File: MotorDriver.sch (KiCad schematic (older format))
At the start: 3 parts, among them P3 +12V, P4 MA, P5 MB

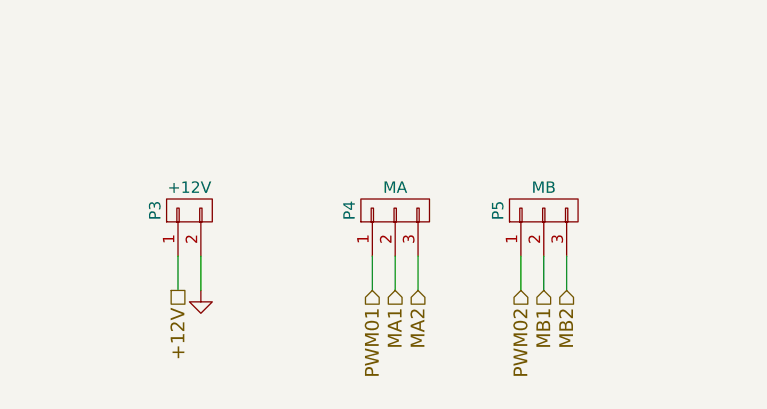
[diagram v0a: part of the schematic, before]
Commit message: Changes to be committed: 	new file:   78LXXSOT89.pdf 	modified:   Control.sch 	modified:   Debugger.sch 	modified:   MotorDriver.sch 	modified:   PS.sch 	modified:   Sensor.sch 	new file:   XL6009-Schematic-Diagram.pdf 	modified:   main-cache.lib 	new file:   main.cmp 	new file:   main.kicad_pcb 	new file:   main.net 	modified:   main.pro 	modified:   main.sch
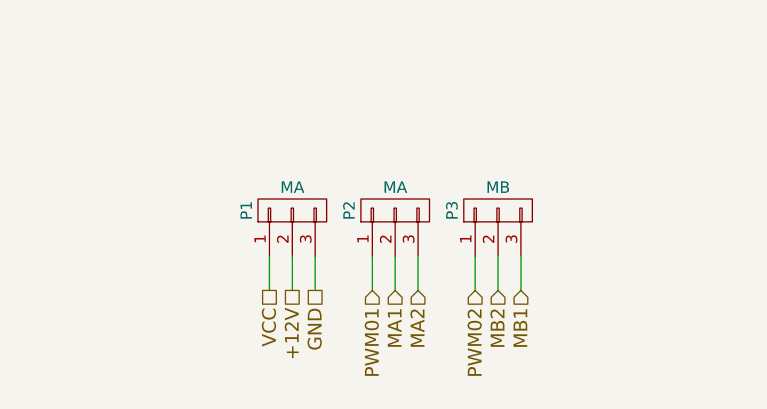
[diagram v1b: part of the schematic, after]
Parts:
- removed P3: +12V, symbol CONN_01X02
- added P1: MA, Pin_Headers:Pin_Header_Straight_1x03, symbol CONN_01X03
- P2: renamed from P4; footprint (none) -> Pin_Headers:Pin_Header_Straight_1x03
- P3: renamed from P5; footprint (none) -> Pin_Headers:Pin_Header_Straight_1x03
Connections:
- net +12V: now also P1.2 (P2)
- net GND: now also P1.3 (P3)
- net MB1: now also P3.3 (P3); no longer P3.2 (P2)
- net MB2: now also P3.2 (P2); no longer P3.3 (P3)
- new net VCC: P1.1 (P1)
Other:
- moved on the sheet: P3
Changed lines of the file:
@@
 EESchema Schematic File Version 2
+LIBS:main-rescue
 LIBS:power
 LIBS:device
@@
 LIBS:contrib
 LIBS:main-cache
+LIBS:tcrt5000
 EELAYER 25 0
 EELAYER END
 $Descr A4 11693 8268
 encoding utf-8
-Sheet 3 6
+Sheet 2 6
 Title ""
 Date ""
@@
 FC BE 3D D5 51 7A EF CF B9 F4 3C 34 7D D1 30 37 C2 0E 7F 80 58 F1 33 ED 6A 46 BF 3F CB 91 FE BE
 6F 63 8E 3F 36 CC D7 84 73 CC F1 9C 31 5F 13 CE 31 C7 73 C6 DC 08 E7 98 E3 39 63 6E 84 73 CC F1
-9C F1 FF 03 32 A2 CC 28 D8 D1 50 57 00 00 00 00 49 45 4E 44 AE 42 60 82 11
+9C F1 FF 03 32 A2 CC 28 D8 D1 50 57 00 00 00 00 49 45 4E 44 AE 42 60 82 31
 EndData
 $EndBitmap
 $Comp
-L CONN_01X02 P3
-U 1 1 558D4ABF
-P 1500 3350
-F 0 "P3" H 1500 3500 50  0000 C CNN
-F 1 "+12V" V 1600 3350 50  0000 C CNN
-F 2 "" H 1500 3350 60  0000 C CNN
-F 3 "" H 1500 3350 60  0000 C CNN
-	1    1500 3350
-	0    -1   -1   0
-$EndComp
-$Comp
-L CONN_01X03 P4
+L CONN_01X03 P2
 U 1 1 558D4B4A
 P 2400 3350
-F 0 "P4" H 2400 3550 50  0000 C CNN
+F 0 "P2" H 2400 3550 50  0000 C CNN
 F 1 "MA" V 2500 3350 50  0000 C CNN
-F 2 "" H 2400 3350 60  0000 C CNN
+F 2 "Pin_Headers:Pin_Header_Straight_1x03" H 2400 3350 60  0001 C CNN
 F 3 "" H 2400 3350 60  0000 C CNN
 	1    2400 3350
@@
 $EndComp
 $Comp
-L CONN_01X03 P5
+L CONN_01X03 P3
 U 1 1 558D4B7D
-P 3050 3350
-F 0 "P5" H 3050 3550 50  0000 C CNN
-F 1 "MB" V 3150 3350 50  0000 C CNN
-F 2 "" H 3050 3350 60  0000 C CNN
-F 3 "" H 3050 3350 60  0000 C CNN
-	1    3050 3350
+P 2850 3350
+F 0 "P3" H 2850 3550 50  0000 C CNN
+F 1 "MB" V 2950 3350 50  0000 C CNN
+F 2 "Pin_Headers:Pin_Header_Straight_1x03" H 2850 3350 60  0001 C CNN
+F 3 "" H 2850 3350 60  0000 C CNN
+	1    2850 3350
 	0    -1   -1   0
 $EndComp
-Text HLabel 1450 3700 3    60   UnSpc ~ 0
+Text HLabel 1950 3700 3    60   UnSpc ~ 0
 +12V
-$Comp
-L GND #PWR06
-U 1 1 558D4F84
-P 1550 3700
-F 0 "#PWR06" H 1550 3700 30  0001 C CNN
-F 1 "GND" H 1550 3630 30  0001 C CNN
-F 2 "" H 1550 3700 60  0000 C CNN
-F 3 "" H 1550 3700 60  0000 C CNN
-	1    1550 3700
-	1    0    0    -1
-$EndComp
 Text HLabel 2300 3700 3    60   Input ~ 0
 PWM01
@@
 Text HLabel 2500 3700 3    60   Input ~ 0
 MA2
-Text HLabel 2950 3700 3    60   Input ~ 0
+Text HLabel 2750 3700 3    60   Input ~ 0
 PWM02
-Text HLabel 3050 3700 3    60   Input ~ 0
+Text HLabel 2950 3700 3    60   Input ~ 0
 MB1
-Text HLabel 3150 3700 3    60   Input ~ 0
+Text HLabel 2850 3700 3    60   Input ~ 0
 MB2
 Wire Wire Line
-	2950 3550 2950 3700
+	2750 3550 2750 3700
 Wire Wire Line
-	3050 3550 3050 3700
+	2850 3550 2850 3700
 Wire Wire Line
-	3150 3550 3150 3700
+	2950 3550 2950 3700
 Wire Wire Line
-	1550 3550 1550 3700
+	2050 3550 2050 3700
 Wire Wire Line
-	1450 3550 1450 3700
+	1950 3550 1950 3700
 Wire Wire Line
 	2300 3550 2300 3700
@@
 Wire Wire Line
 	2500 3550 2500 3700
+Text HLabel 2050 3700 3    60   UnSpc ~ 0
+GND
+$Comp
+L CONN_01X03 P1
+U 1 1 558D6CE8
+P 1950 3350
+F 0 "P1" H 1950 3550 50  0000 C CNN
+F 1 "MA" V 2050 3350 50  0000 C CNN
+F 2 "Pin_Headers:Pin_Header_Straight_1x03" H 1950 3350 60  0001 C CNN
+F 3 "" H 1950 3350 60  0000 C CNN
+	1    1950 3350
+	0    -1   -1   0
+$EndComp
+Text HLabel 1850 3700 3    60   UnSpc ~ 0
+VCC
+Wire Wire Line
+	1850 3550 1850 3700
 $EndSCHEMATC

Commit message: update
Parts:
- P1: value MA -> MP
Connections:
- net PWM01: now also P3.1 (P1); no longer P2.1 (P1)
- net PWM02: now also P2.1 (P1); no longer P3.1 (P1)
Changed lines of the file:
@@
 LIBS:memory
 LIBS:xilinx
-LIBS:special
 LIBS:microcontrollers
 LIBS:dsp
@@
 encoding utf-8
 Sheet 2 6
-Title ""
-Date ""
-Rev ""
+Title "KENZANIN LINEFOLLOWER"
+Date "2015-06-28"
+Rev "1.0"
 Comp ""
 Comment1 ""
@@
 FC BE 3D D5 51 7A EF CF B9 F4 3C 34 7D D1 30 37 C2 0E 7F 80 58 F1 33 ED 6A 46 BF 3F CB 91 FE BE
 6F 63 8E 3F 36 CC D7 84 73 CC F1 9C 31 5F 13 CE 31 C7 73 C6 DC 08 E7 98 E3 39 63 6E 84 73 CC F1
-9C F1 FF 03 32 A2 CC 28 D8 D1 50 57 00 00 00 00 49 45 4E 44 AE 42 60 82 31
+9C F1 FF 03 32 A2 CC 28 D8 D1 50 57 00 00 00 00 49 45 4E 44 AE 42 60 82 E5
 EndData
 $EndBitmap
@@
 Text HLabel 1950 3700 3    60   UnSpc ~ 0
 +12V
-Text HLabel 2300 3700 3    60   Input ~ 0
+Text HLabel 2750 3700 3    60   Input ~ 0
 PWM01
 Text HLabel 2400 3700 3    60   Input ~ 0
@@
 Text HLabel 2500 3700 3    60   Input ~ 0
 MA2
-Text HLabel 2750 3700 3    60   Input ~ 0
+Text HLabel 2300 3700 3    60   Input ~ 0
 PWM02
 Text HLabel 2950 3700 3    60   Input ~ 0
@@
 P 1950 3350
 F 0 "P1" H 1950 3550 50  0000 C CNN
-F 1 "MA" V 2050 3350 50  0000 C CNN
+F 1 "MP" V 2050 3350 50  0000 C CNN
 F 2 "Pin_Headers:Pin_Header_Straight_1x03" H 1950 3350 60  0001 C CNN
 F 3 "" H 1950 3350 60  0000 C CNN
